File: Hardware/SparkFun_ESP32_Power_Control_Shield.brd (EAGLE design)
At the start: 101.6 x 50.8 mm, 66 parts, among them IC1 OP-AMP, IC2 OP-AMP, J1 5.5x2.1mm Barrel, U1 MC33926, U2 MC33926, U3 MC33926, U4 LM317

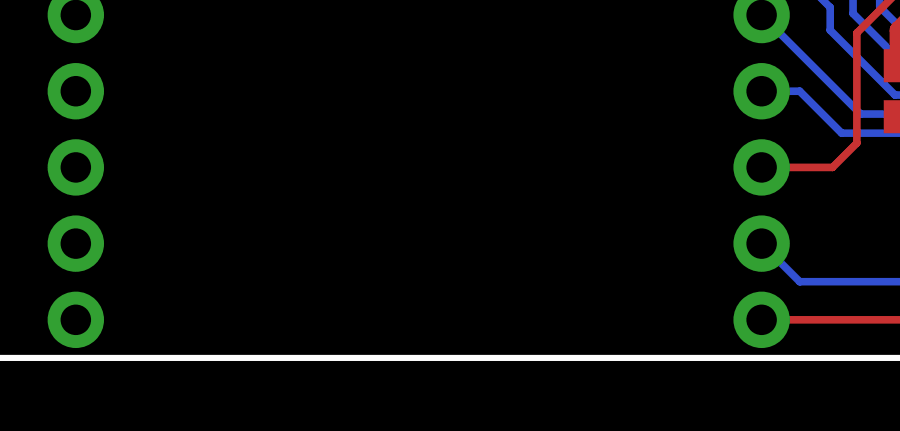
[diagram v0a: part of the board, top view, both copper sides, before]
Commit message: Added measurements for board size and version number
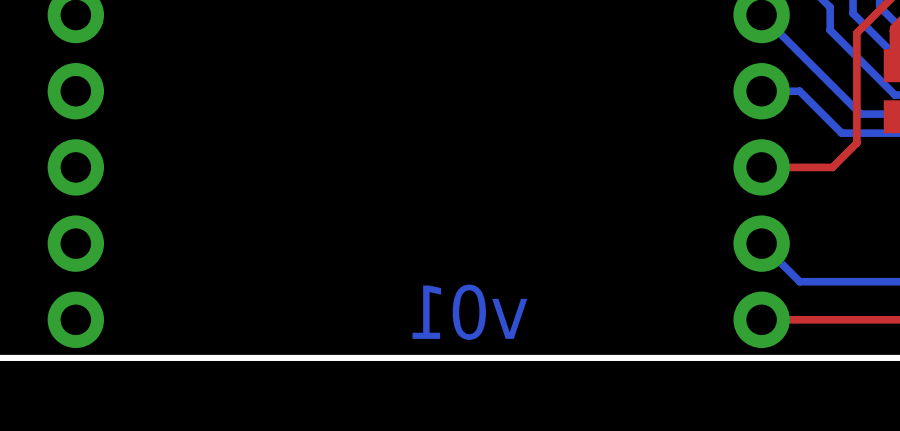
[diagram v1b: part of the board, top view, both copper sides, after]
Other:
- board text added: "Alex Wende"
- board text added: "Units are in Inches"
- board text added: "v01"
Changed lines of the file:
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@@
 <layer number="20" name="Dimension" color="15" fill="1" visible="yes" active="yes"/>
 <layer number="21" name="tPlace" color="16" fill="1" visible="yes" active="yes"/>
-<layer number="22" name="bPlace" color="14" fill="1" visible="no" active="yes"/>
+<layer number="22" name="bPlace" color="14" fill="1" visible="yes" active="yes"/>
 <layer number="23" name="tOrigins" color="15" fill="1" visible="yes" active="yes"/>
-<layer number="24" name="bOrigins" color="15" fill="1" visible="no" active="yes"/>
+<layer number="24" name="bOrigins" color="15" fill="1" visible="yes" active="yes"/>
 <layer number="25" name="tNames" color="7" fill="1" visible="no" active="yes"/>
 <layer number="26" name="bNames" color="7" fill="1" visible="no" active="yes"/>
@@
 <layer number="37" name="tTest" color="7" fill="1" visible="no" active="yes"/>
 <layer number="38" name="bTest" color="7" fill="1" visible="no" active="yes"/>
-<layer number="39" name="tKeepout" color="4" fill="11" visible="no" active="yes"/>
-<layer number="40" name="bKeepout" color="1" fill="11" visible="no" active="yes"/>
+<layer number="39" name="tKeepout" color="4" fill="11" visible="yes" active="yes"/>
+<layer number="40" name="bKeepout" color="1" fill="11" visible="yes" active="yes"/>
 <layer number="41" name="tRestrict" color="4" fill="10" visible="no" active="yes"/>
 <layer number="42" name="bRestrict" color="1" fill="10" visible="no" active="yes"/>
 <layer number="43" name="vRestrict" color="2" fill="10" visible="no" active="yes"/>
 <layer number="44" name="Drills" color="7" fill="1" visible="no" active="yes"/>
-<layer number="45" name="Holes" color="7" fill="1" visible="no" active="yes"/>
+<layer number="45" name="Holes" color="7" fill="1" visible="yes" active="yes"/>
 <layer number="46" name="Milling" color="3" fill="1" visible="no" active="yes"/>
-<layer number="47" name="Measures" color="7" fill="1" visible="no" active="yes"/>
+<layer number="47" name="Measures" color="7" fill="1" visible="yes" active="yes"/>
 <layer number="48" name="Document" color="7" fill="1" visible="no" active="yes"/>
 <layer number="49" name="Reference" color="7" fill="1" visible="no" active="yes"/>
@@
 <wire x1="10.16" y1="43.688" x2="10.16" y2="50.165" width="0.4064" layer="21"/>
 <text x="13.208" y="45.085" size="1.27" layer="21" font="vector" ratio="15" rot="R90">BATT</text>
+<text x="44.45" y="-22.86" size="1.778" layer="51" font="vector" ratio="15">Alex Wende</text>
+<dimension x1="98.425" y1="3.175" x2="101.6" y2="3.175" x3="100.0125" y3="-5.08" textsize="1.778" textratio="15" layer="47" unit="inch" precision="3"/>
+<dimension x1="98.425" y1="3.175" x2="3.175" y2="3.175" x3="50.8" y3="-5.08" textsize="1.778" textratio="15" layer="47" unit="inch" precision="3"/>
+<dimension x1="3.175" y1="3.175" x2="0" y2="3.175" x3="1.5875" y3="-5.08" textsize="1.778" textratio="15" layer="47" unit="inch" precision="3"/>
+<dimension x1="3.175" y1="3.175" x2="3.175" y2="0" x3="-5.08" y3="1.5875" textsize="1.778" textratio="15" layer="47" unit="inch" precision="3"/>
+<dimension x1="3.175" y1="3.175" x2="3.175" y2="47.625" x3="-5.08" y3="25.4" textsize="1.778" textratio="15" layer="47" unit="inch" precision="3"/>
+<dimension x1="3.175" y1="47.625" x2="3.175" y2="50.8" x3="-5.08" y3="49.2125" textsize="1.778" textratio="15" layer="47" unit="inch" precision="3"/>
+<text x="36.83" y="-8.89" size="1.778" layer="47" font="vector" ratio="15">Units are in Inches</text>
+<text x="22.733" y="0.635" size="1.778" layer="16" font="vector" ratio="15" rot="MR0">v01</text>
 </plain>
 <attributes>

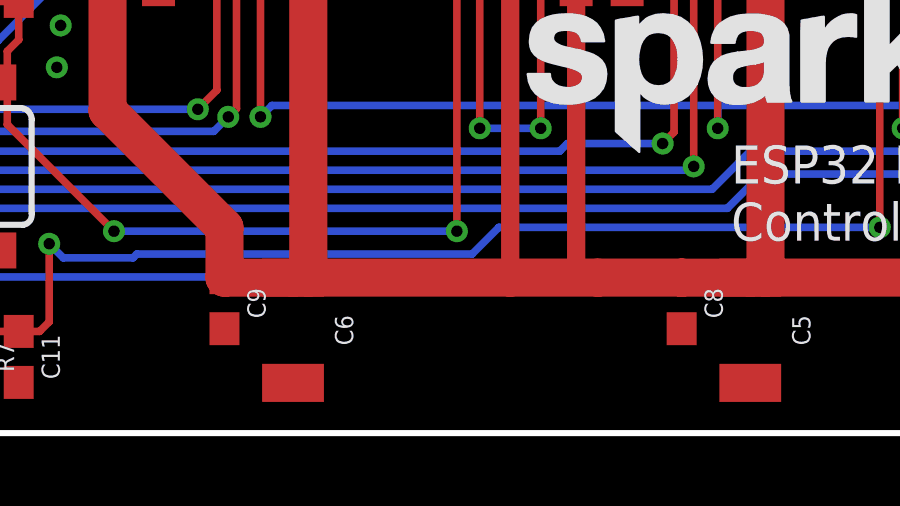
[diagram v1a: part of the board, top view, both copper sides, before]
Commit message: Added external capacitor
External capacitor will be populated by end user if too much ripple is
present on power rail.
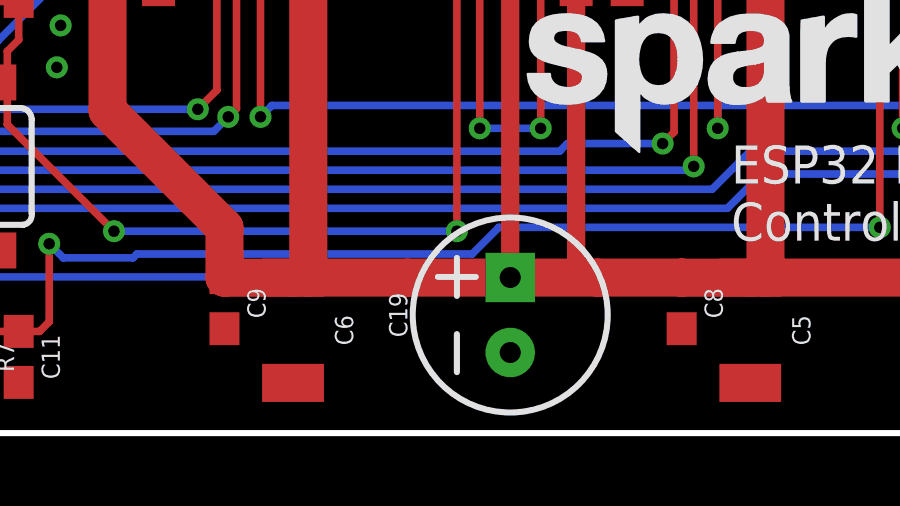
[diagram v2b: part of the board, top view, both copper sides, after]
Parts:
- added C19: Ext., SparkFun-Capacitors:CPOL-RADIAL-2.5MM-6.5MM
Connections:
- net GND: now also C19.2
- net VCC: now also C19.1
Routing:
- net VCC: track 292.3 -> 295.8 mm
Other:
- board text added: "I-Sense 2 (38)"
- board text added: "I-Sense 4 (37)"
- board text added: "I-Sense 6 (36)"
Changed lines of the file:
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@@
 <layer number="22" name="bPlace" color="14" fill="1" visible="yes" active="yes"/>
 <layer number="23" name="tOrigins" color="15" fill="1" visible="yes" active="yes"/>
-<layer number="24" name="bOrigins" color="15" fill="1" visible="yes" active="yes"/>
+<layer number="24" name="bOrigins" color="15" fill="1" visible="no" active="yes"/>
 <layer number="25" name="tNames" color="7" fill="1" visible="no" active="yes"/>
 <layer number="26" name="bNames" color="7" fill="1" visible="no" active="yes"/>
@@
 <layer number="37" name="tTest" color="7" fill="1" visible="no" active="yes"/>
 <layer number="38" name="bTest" color="7" fill="1" visible="no" active="yes"/>
-<layer number="39" name="tKeepout" color="4" fill="11" visible="yes" active="yes"/>
-<layer number="40" name="bKeepout" color="1" fill="11" visible="yes" active="yes"/>
+<layer number="39" name="tKeepout" color="4" fill="11" visible="no" active="yes"/>
+<layer number="40" name="bKeepout" color="1" fill="11" visible="no" active="yes"/>
 <layer number="41" name="tRestrict" color="4" fill="10" visible="no" active="yes"/>
 <layer number="42" name="bRestrict" color="1" fill="10" visible="no" active="yes"/>
 <layer number="43" name="vRestrict" color="2" fill="10" visible="no" active="yes"/>
 <layer number="44" name="Drills" color="7" fill="1" visible="no" active="yes"/>
-<layer number="45" name="Holes" color="7" fill="1" visible="yes" active="yes"/>
+<layer number="45" name="Holes" color="7" fill="1" visible="no" active="yes"/>
 <layer number="46" name="Milling" color="3" fill="1" visible="no" active="yes"/>
-<layer number="47" name="Measures" color="7" fill="1" visible="yes" active="yes"/>
+<layer number="47" name="Measures" color="7" fill="1" visible="no" active="yes"/>
 <layer number="48" name="Document" color="7" fill="1" visible="no" active="yes"/>
 <layer number="49" name="Reference" color="7" fill="1" visible="no" active="yes"/>
@@
 <text x="36.83" y="-8.89" size="1.778" layer="47" font="vector" ratio="15">Units are in Inches</text>
 <text x="22.733" y="0.635" size="1.778" layer="16" font="vector" ratio="15" rot="MR0">v01</text>
+<text x="31.75" y="1.27" size="0.8128" layer="22" font="vector" ratio="15" rot="MR180" align="center-left">I-Sense 6 (36)</text>
+<text x="31.75" y="3.81" size="0.8128" layer="22" font="vector" ratio="15" rot="MR180" align="center-left">I-Sense 4 (37)</text>
+<text x="31.75" y="6.35" size="0.8128" layer="22" font="vector" ratio="15" rot="MR180" align="center-left">I-Sense 2 (38)</text>
 </plain>
 <attributes>
@@
 <attribute name="SF_ID" value="DEV-13907" x="31.75" y="50.8" size="1.778" layer="27" font="vector" ratio="15" rot="R180" display="off"/>
 </element>
+<element name="C19" library="SparkFun-Capacitors" package="CPOL-RADIAL-2.5MM-6.5MM" value="Ext." x="66.929" y="3.937" rot="R90">
+<attribute name="PROD_ID" value="CAP-08439" x="66.929" y="3.937" size="0.8128" layer="27" font="vector" ratio="15" rot="R90" display="off"/>
+</element>
 </elements>
 <signals>
@@
 <wire x1="72.644" y1="5.184" x2="69.85" y2="5.184" width="1.27" layer="1"/>
 <wire x1="69.85" y1="5.184" x2="66.929" y2="5.184" width="1.27" layer="1"/>
-<wire x1="66.929" y1="5.184" x2="60.198" y2="5.184" width="1.27" layer="1"/>
+<wire x1="66.929" y1="5.184" x2="63.5" y2="5.184" width="1.27" layer="1"/>
+<wire x1="63.5" y1="5.184" x2="60.198" y2="5.184" width="1.27" layer="1"/>
 <wire x1="60.198" y1="5.184" x2="59.69" y2="5.184" width="1.27" layer="1"/>
 <wire x1="59.69" y1="5.184" x2="59.69" y2="5.1807" width="1.27" layer="1"/>
@@
 <wire x1="66.548" y1="5.184" x2="66.929" y2="5.184" width="0.6096" layer="1"/>
 <wire x1="52.2022" y1="44.45" x2="52.2022" y2="46.99" width="1.27" layer="1"/>
+<contactref element="C19" pad="1"/>
+<wire x1="66.929" y1="5.187" x2="63.503" y2="5.187" width="0.254" layer="1"/>
+<wire x1="63.503" y1="5.187" x2="63.5" y2="5.184" width="0.254" layer="1"/>
 </signal>
 <signal name="GND">
@@
 <via x="51.816" y="12.192" extent="1-16" drill="0.381"/>
 <via x="51.943" y="13.589" extent="1-16" drill="0.381"/>
+<contactref element="C19" pad="2"/>
 </signal>
 <signal name="P_OUT2">

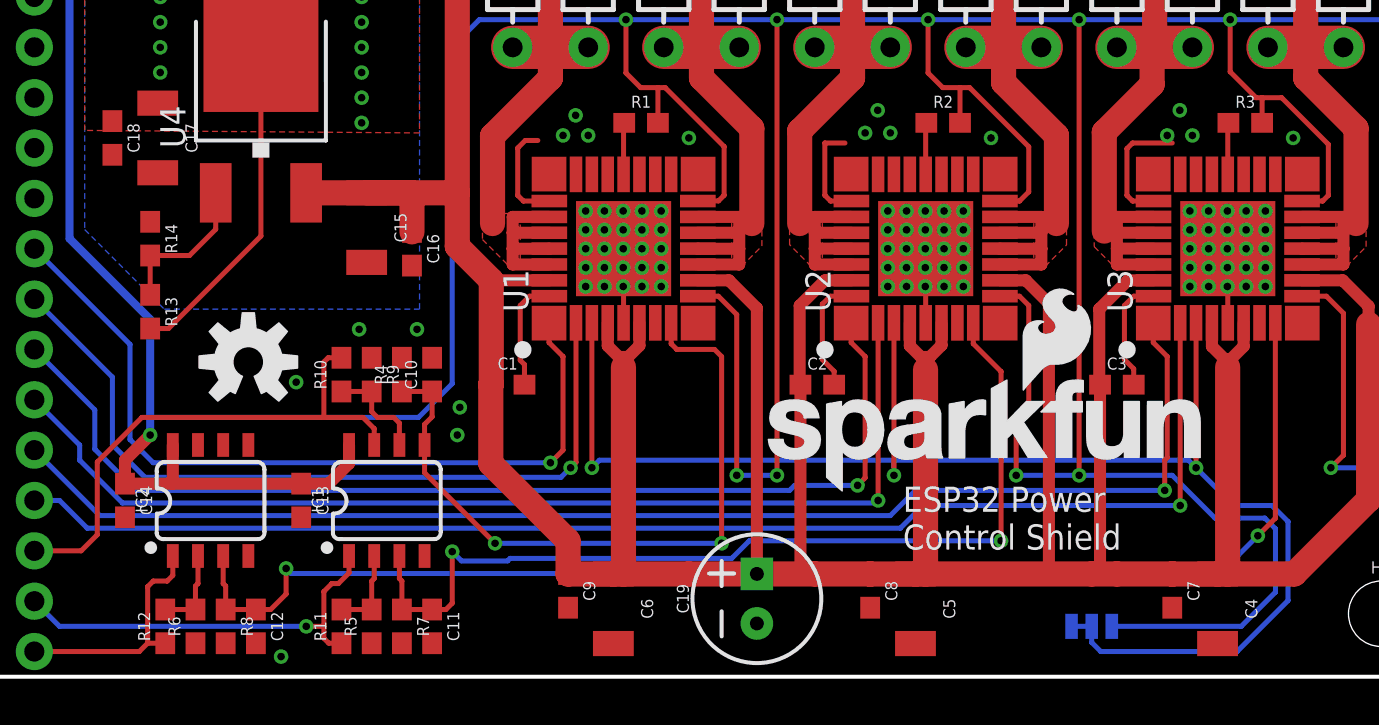
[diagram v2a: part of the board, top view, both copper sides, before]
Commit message: Proto design review changes
- Replaced SMD barrel jack with PTH
- Replaced op-amp resistor with 15k resistor
- Moved IO away from pins 34-39
- Attached disable input pin to IO pin
- Replaced 3/4 2-pin screw terminals with 6-pin screw terminal
- Added labeling to all IO pins used
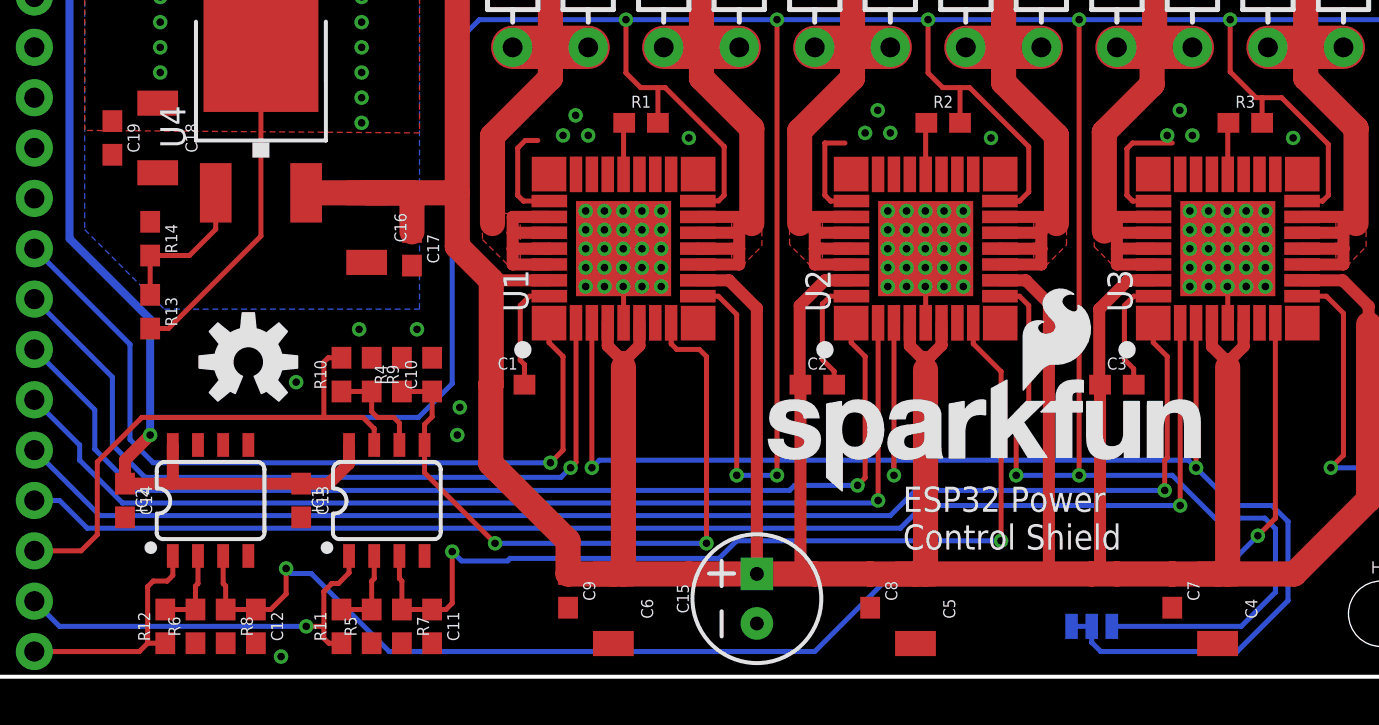
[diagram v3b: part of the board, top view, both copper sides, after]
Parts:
- C15: value 10uF -> Ext.; device SparkFun-Capacitors:1210 -> SparkFun-Capacitors:CPOL-RADIAL-2.5MM-6.5MM
- C16, C18: value 0.1uF -> 10uF; device SparkFun-Capacitors:0603 -> SparkFun-Capacitors:1210
- C17: value 10uF -> 0.1uF; device SparkFun-Capacitors:1210 -> SparkFun-Capacitors:0603
- C19: value Ext. -> 0.1uF; device SparkFun-Capacitors:CPOL-RADIAL-2.5MM-6.5MM -> SparkFun-Capacitors:0603
- R11: value 390 -> 15k
- U1, U2, U3: device Power_Control_Adapter_Temp:32-PQFN -> SparkFun_ESP32_Power_Control_Shield_Temp:32-PQFN
- moved C19 40.0 mm to (34.4, 27.2), turned to 270 degrees
- moved C15 27.2 mm to (66.9, 3.94), turned to 90 degrees
- moved C17 14.0 mm to (49.5, 21.6)
- moved C16 2.52 mm to (47.2, 22.7)
- moved C18 2.29 mm to (36.7, 27.2)
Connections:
- net 5V: now also C19.1; no longer C17.1
- net VCC: now also C17.1; no longer C19.1
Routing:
- net I_SENSE3: track 68.4 -> 71.7 mm
- net I_SENSE1: track 35.5 -> 34.0 mm
